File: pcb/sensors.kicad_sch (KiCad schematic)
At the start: 22 parts, among them J2 Conn_01x04_Pin, Q1 BSS138, Q2 BSS138, U3 BME280, U4 SGP30-2.5K

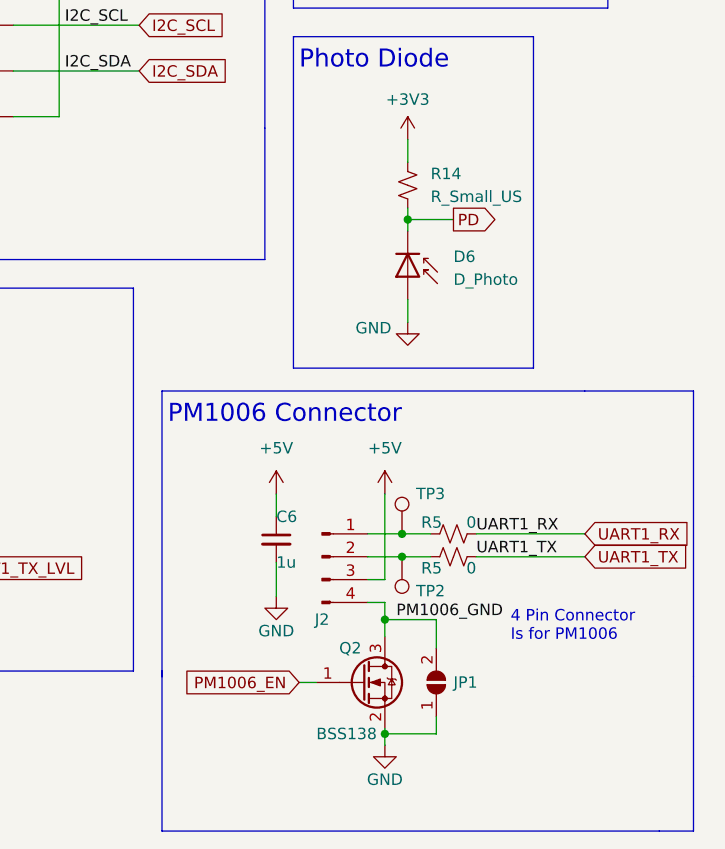
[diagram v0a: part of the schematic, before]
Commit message: update the pcb to include the updated schematic for the PD and the TPM moudle
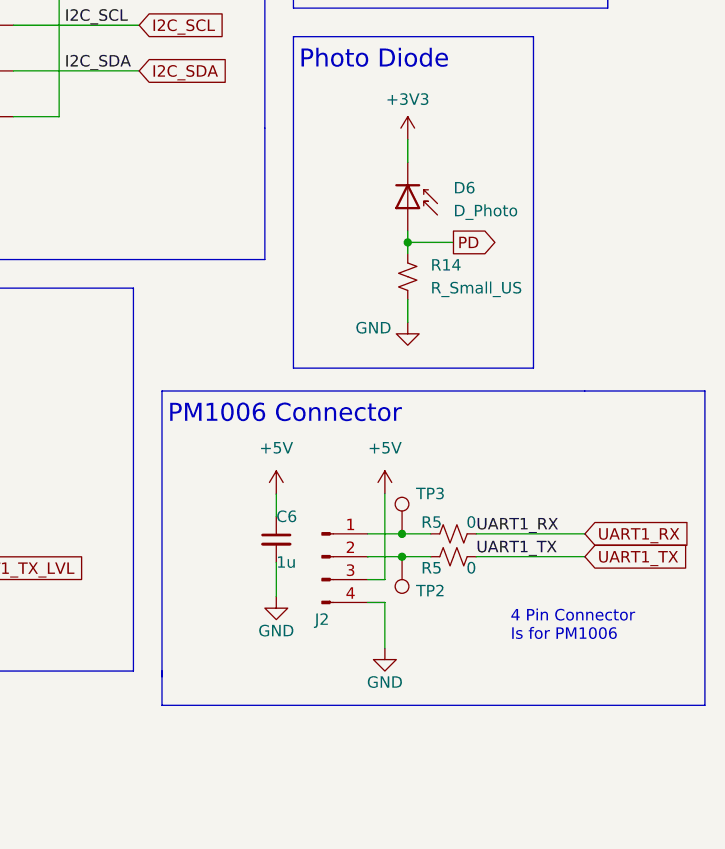
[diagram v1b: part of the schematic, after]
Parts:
- removed JP1: SolderJumper_2_Open, Jumper:SolderJumper-2_P1.3mm_Open_RoundedPad1.0x1.5mm, symbol Jumper:SolderJumper_2_Open
- removed Q2: BSS138, Package_TO_SOT_SMD:SOT-23, symbol Transistor_FET:BSS138
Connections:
- net PM1006_GND is gone; now on net GND: J2.4 (Pin_4)
- net +3V3: now also D6.1 (K); no longer R14.2
- net GND: now also R14.1; no longer D6.2 (A)
- net PD: now also D6.2 (A), R14.2; no longer D6.1 (K), R14.1
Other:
- moved on the sheet: D6, R14

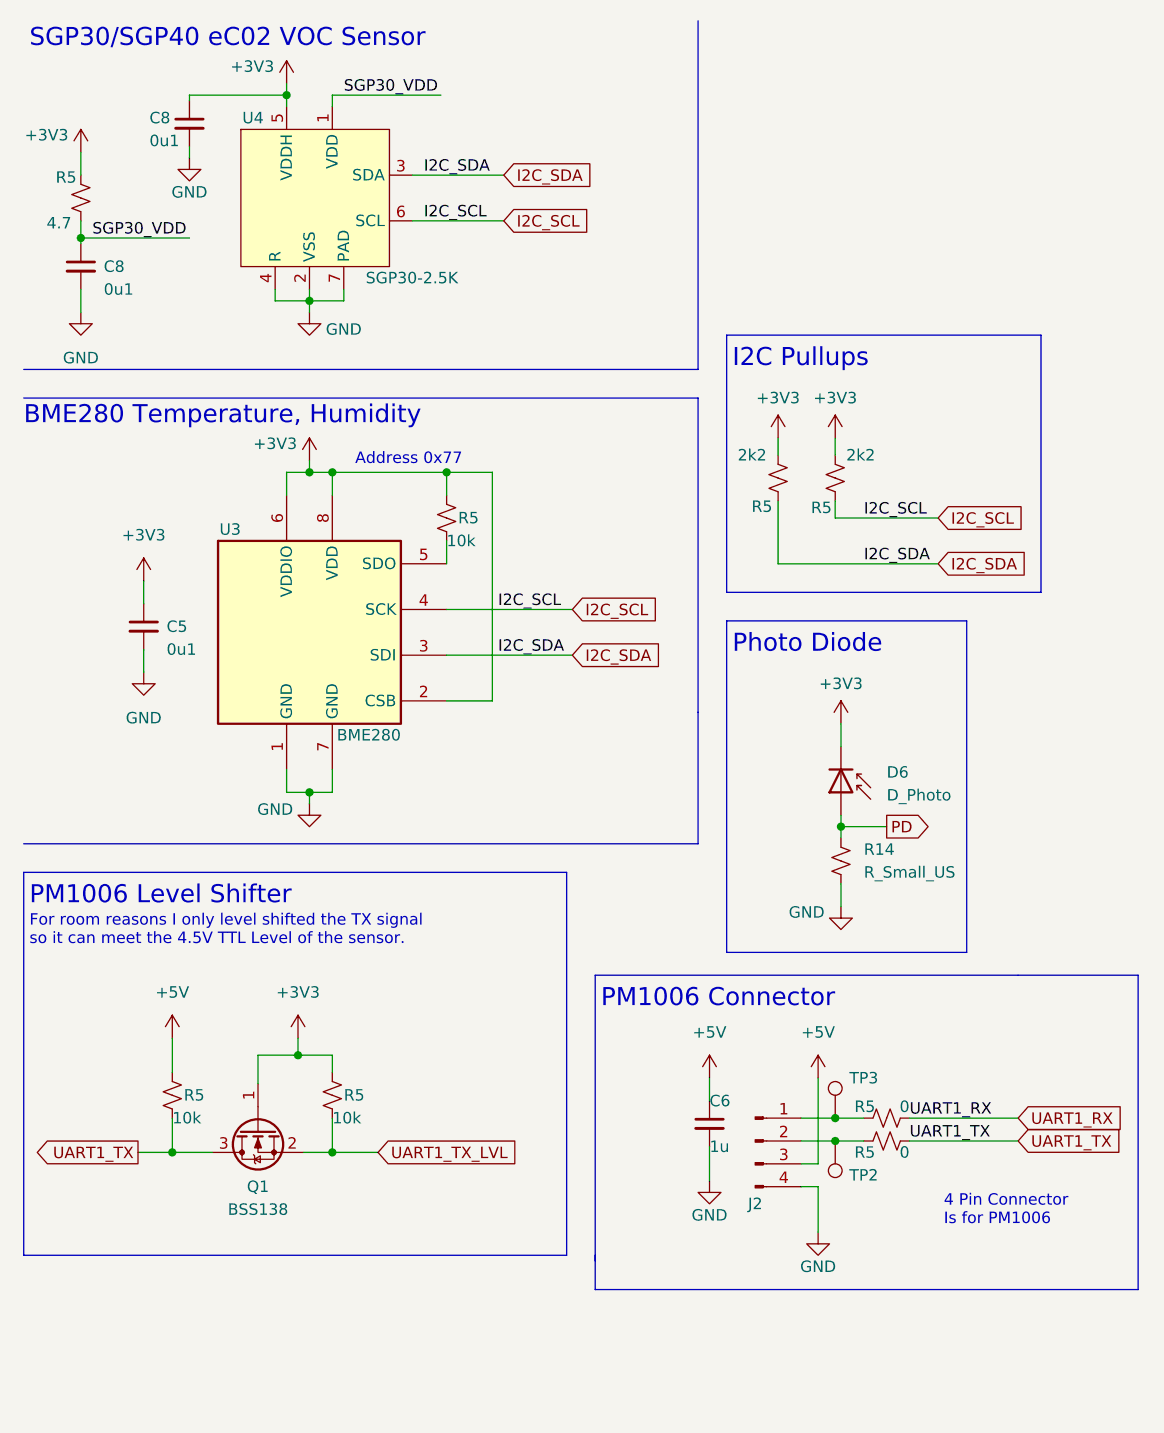
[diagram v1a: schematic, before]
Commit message: Add new plugins for BOM and PNP file management
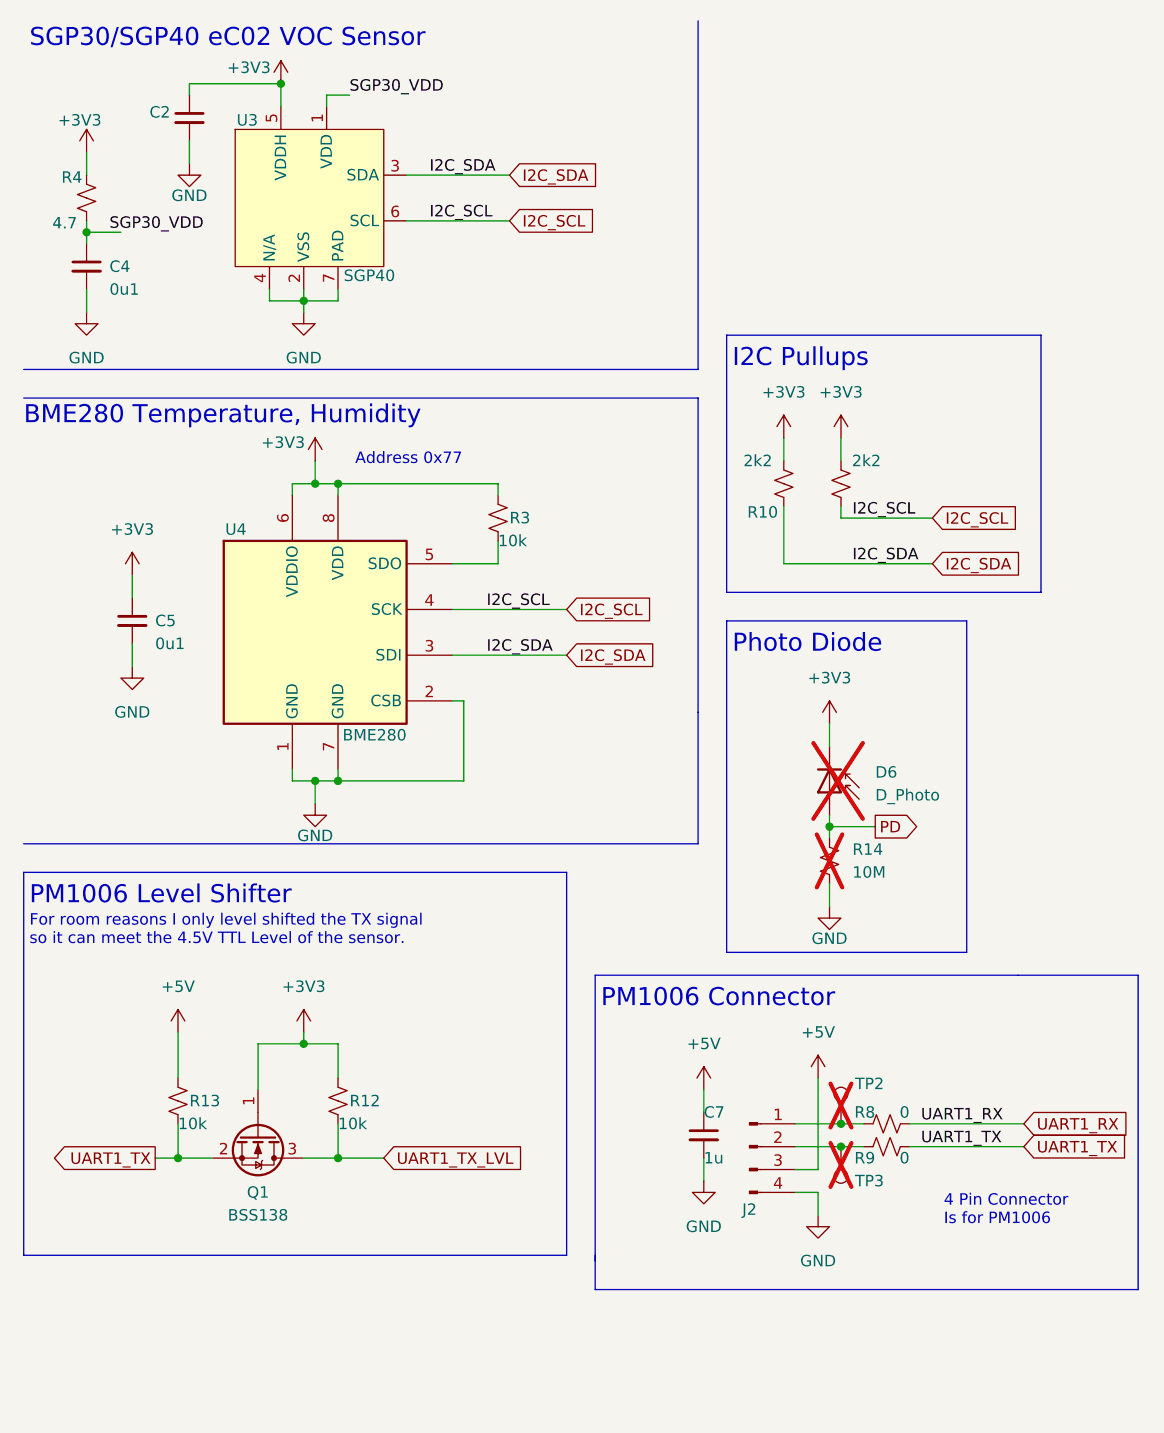
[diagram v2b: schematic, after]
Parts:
- removed U4: SGP30-2.5K, Kevin_Lutzer_Lbr:SGP30-2.5K_SEN, symbol Kevin_Lutzer_Lbr:SGP30-2.5K
- added U3: SGP40, Kevin_Lutzer_Lbr:SGP30-2.5K_SEN-M, symbol Kevin_Lutzer_Lbr:SGP40
- C2, C4: renamed from C8; DNP (none) -> C1590
- C5: DNP (none) -> C1590
- C7: renamed from C6; DNP (none) -> C1592
- D6: now not fitted; now left out of the parts list
- J2: DNP (none) -> C265083
- Q1: DNP (none) -> C52895
- R10, R11: renamed from R5; DNP (none) -> C4190
- R12, R13, R3: renamed from R5; DNP (none) -> C15401
- R14: value R_Small_US -> 10M; now not fitted; now left out of the parts list
- R4: renamed from R5; DNP (none) -> C23162
- R8, R9: renamed from R5; DNP (none) -> C15402
- TP2: renamed from TP3; now not fitted; now left out of the parts list
- TP3: renamed from TP2; now not fitted; now left out of the parts list
- U4: renamed from U3; DNP (none) -> C92489
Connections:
- net +3V3: now also U3.5 (VDDH); no longer U4.2 (CSB)
- net GND: now also U4.2 (CSB), U3.2 (VSS), U3.4 (N/A), U3.7 (PAD)
- net I2C_SCL: now also U3.6 (SCL)
- net I2C_SDA: now also U3.3 (SDA)
- net SGP30_VDD: now also U3.1 (VDD)
- net UART1_TX: now also Q1.2 (S); no longer Q1.3 (D)
- net UART1_TX_LVL: now also Q1.3 (D); no longer Q1.2 (S)
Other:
- moved on the sheet: C2, C4, C5, C7, J2, R10, R12, R13, R3, R4, R8, R9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

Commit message: make some more progress
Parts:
- added TP5, TP6: TestPoint, TestPoint:TestPoint_Pad_D1.0mm, symbol Connector:TestPoint
- R4: DNP C23162 -> C23164
- U3: DNP (none) -> C2874215
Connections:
- net I2C_SCL: now also TP6.1
- net I2C_SDA: now also TP5.1
- net UART1_TX: now also Q1.3 (D); no longer Q1.2 (S)
- net UART1_TX_LVL: now also Q1.2 (S); no longer Q1.3 (D)
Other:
- moved on the sheet: Q1, R10

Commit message: merge in main
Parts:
- TP5, TP6: now not fitted; now left out of the parts list
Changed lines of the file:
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@@
 		(unit 1)
 		(exclude_from_sim no)
-		(in_bom yes)
-		(on_board yes)
-		(dnp no)
+		(in_bom no)
+		(on_board yes)
+		(dnp yes)
 		(property "Reference" "TP6"
 			(at 121.285 59.055 0)
@@
 			)
 		)
-		(property "LCSC" ""
-			(at 92.71 137.16 0)
-			(effects
-				(font
-					(size 1.27 1.27)
-				)
-				(hide yes)
-			)
-		)
-		(property "MPN" ""
-			(at 92.71 137.16 0)
-			(effects
-				(font
-					(size 1.27 1.27)
-				)
-				(hide yes)
-			)
-		)
 		(pin "1"
 		)
@@
 		(unit 1)
 		(exclude_from_sim no)
-		(in_bom yes)
-		(on_board yes)
-		(dnp no)
+		(in_bom no)
+		(on_board yes)
+		(dnp yes)
 		(property "Reference" "TP5"
 			(at 114.935 73.025 0)

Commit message: do the reroute for the larger ESP32 module
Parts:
- removed TP2, TP3, TP5, TP6: TestPoint, TestPoint:TestPoint_Pad_D1.0mm, symbol Connector:TestPoint
